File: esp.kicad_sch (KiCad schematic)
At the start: 14 parts, among them U2 ESP32-C3-MINI-1U-N4, Y1 SC32S-7PF20PPM

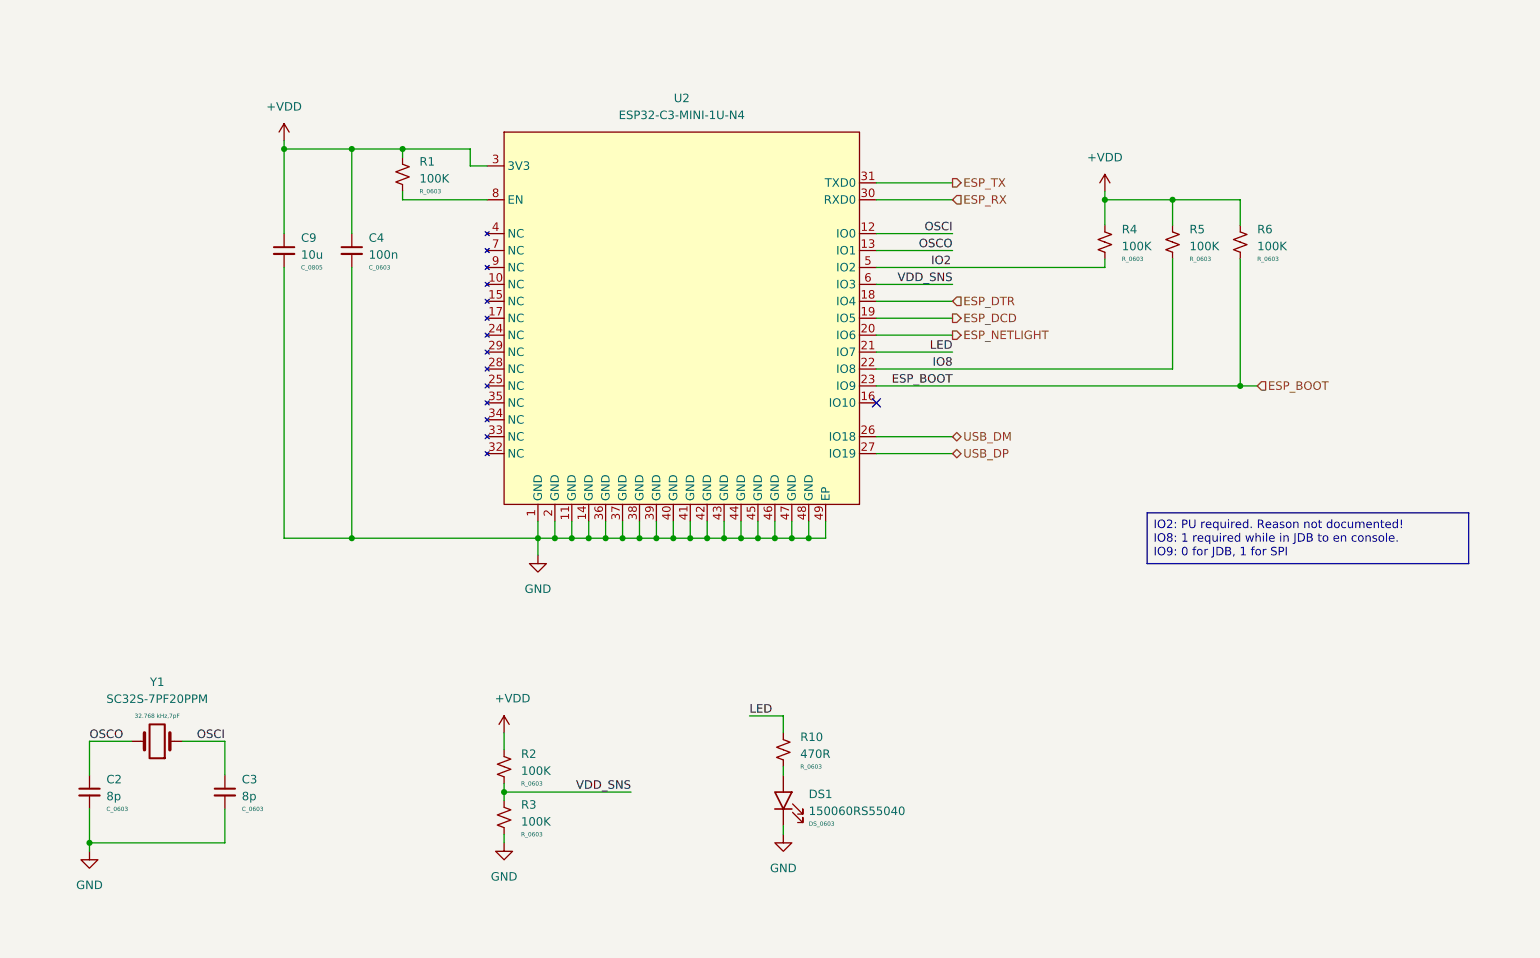
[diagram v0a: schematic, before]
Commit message: Overhaul for buck-boost converter
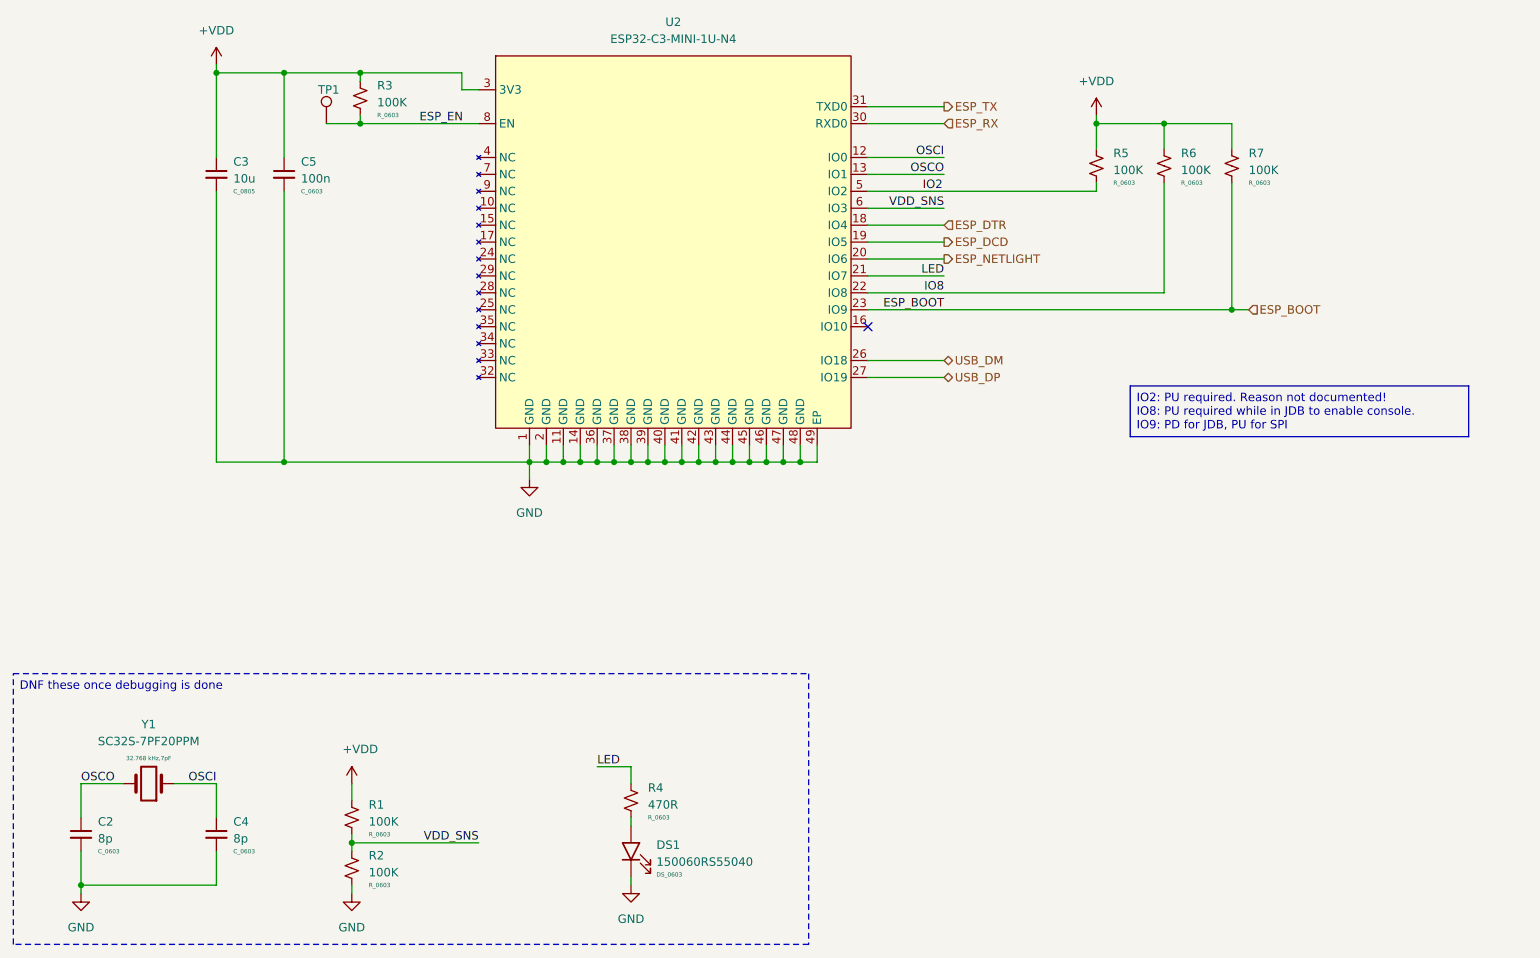
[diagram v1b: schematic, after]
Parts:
- added TP1: ~, TP_TestPoint:TestPoint_1mm, symbol TP_TestPoint:TestPoint_1mm
- renumbered C9 to C3, C3 to C4, C4 to C5, R2 to R1, R3 to R2, R1 to R3, R10 to R4, R4 to R5, R5 to R6, R6 to R7
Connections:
- net ESP_EN: now reaches R3.2, U2.8 (EN)
- net ESP_EN: now also TP1.1
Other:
- company: (none) -> TL Embedded
- title: (none) -> Winglet-ESP
- moved on the sheet: C2, C3, C4, C5, DS1, R1, R2, R3, R4, R5, R6, R7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
